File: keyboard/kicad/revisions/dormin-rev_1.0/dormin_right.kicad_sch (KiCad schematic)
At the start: 104 parts, among them J6_R1 Conn_01x04, Q3_R1 AO3407A, Q4_R1 AO3400A, SW21 SW_Push, SW22 SW_Push, SW23 SW_Push, SW24 SW_Push, SW25 SW_Push, SW26 SW_Push, SW27 SW_Push, SW28 SW_Push, SW29 SW_Push, SW30 SW_Push, SW31 SW_Push, SW32 SW_Push, SW33 SW_Push, SW34 SW_Push, SW35 SW_Push, SW36 SW_Push, SW37 SW_Push, SW38 SW_Push, SW39 SW_Push, SW40 SW_Push, U2 Seeeduino Xiao nRF52840

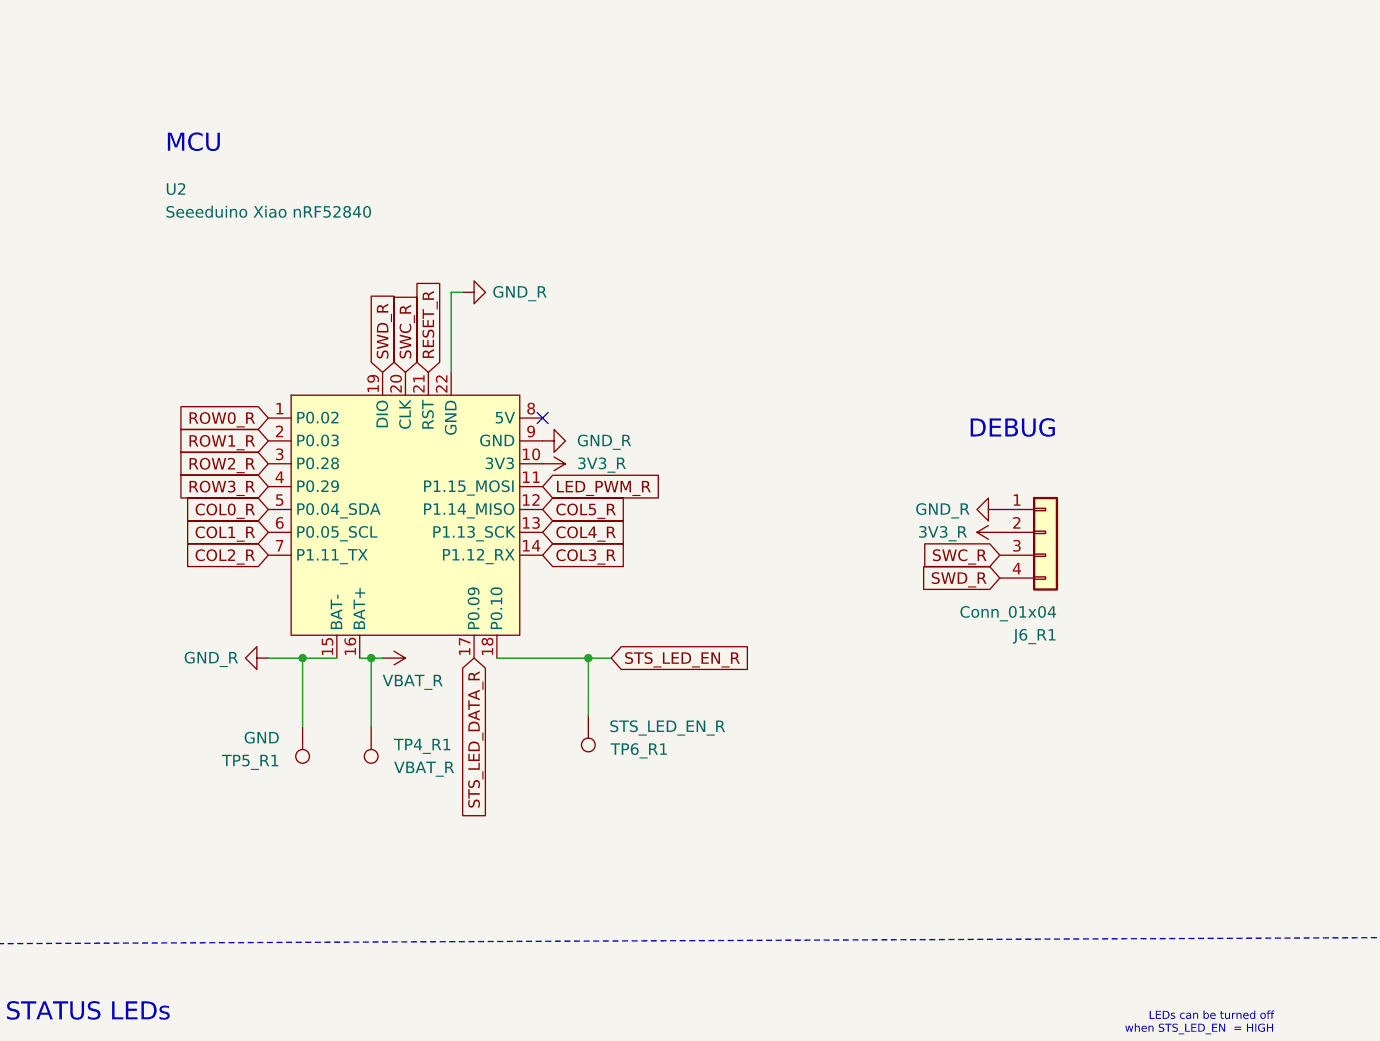
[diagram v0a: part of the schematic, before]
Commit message: refactor: fix xiao footprint and symbol
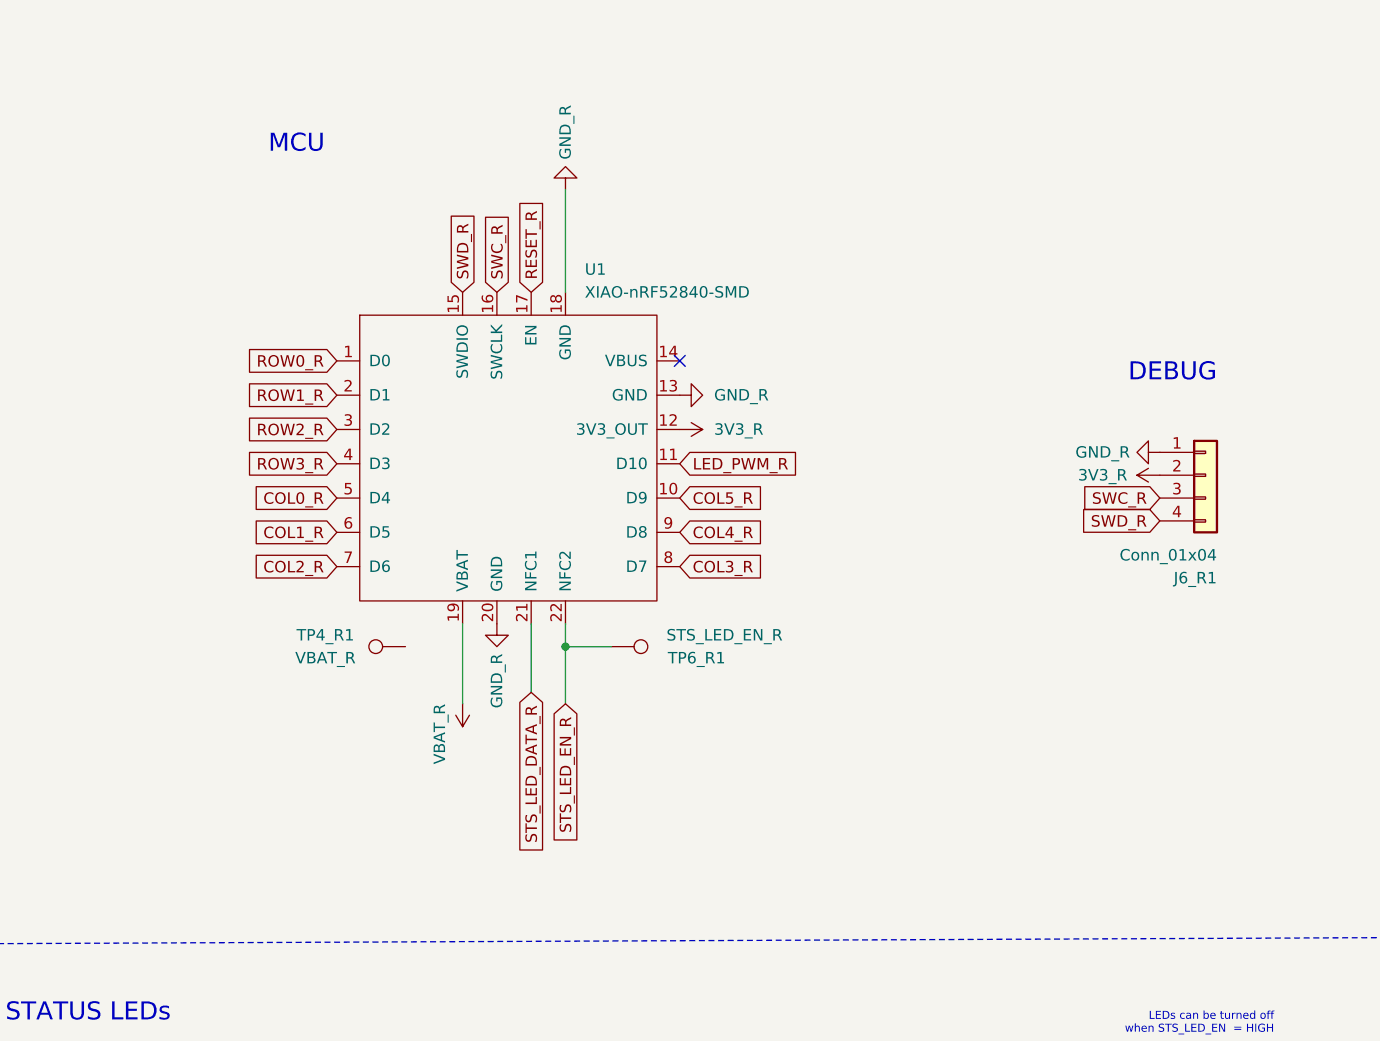
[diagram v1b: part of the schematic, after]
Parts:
- removed TP5_R1: GND, TestPoint:TestPoint_Pad_D1.0mm, symbol Connector:TestPoint
- removed U2: Seeeduino Xiao nRF52840, Seeed_Studio_XIAO_Series:XIAO-nRF52840-SMD, symbol PCM_marbastlib-promicroish:Seeeduino_Xiao_nRF52840
- added U1: XIAO-nRF52840-SMD, Seeed_Studio_XIAO_Series:XIAO-nRF52840-SMD, symbol Seeed_Studio_XIAO_Series:XIAO-nRF52840-SMD
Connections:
- net 3V3_R: now also U1.12 (3V3_OUT)
- net COL0_R: now also U1.5 (D4)
- net COL1_R: now also U1.6 (D5)
- net COL2_R: now also U1.7 (D6)
- net COL3_R: now also U1.8 (D7)
- net COL4_R: now also U1.9 (D8)
- net COL5_R: now also U1.10 (D9)
- net GND_R: now also U1.13 (GND), U1.18 (GND), U1.20 (GND)
- net LED_PWM_R: now also U1.11 (D10)
- net RESET_R: now also U1.17 (EN)
- net ROW0_R: now also U1.1 (D0)
- net ROW1_R: now also U1.2 (D1)
- net ROW2_R: now also U1.3 (D2)
- net ROW3_R: now also U1.4 (D3)
- net STS_LED_DATA_R: now also U1.21 (NFC1)
- net STS_LED_EN_R: now also U1.22 (NFC2)
- net SWC_R: now also U1.16 (SWCLK)
- net SWD_R: now also U1.15 (SWDIO)
- net VBAT_R: now also U1.19 (VBAT); no longer TP4_R1.1
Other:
- moved on the sheet: J6_R1
